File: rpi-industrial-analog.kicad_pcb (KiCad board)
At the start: 2 copper layers, 88.4 x 50 mm, 74 parts, among them J101 CONN_01X04, J102 CONN_01X08, U101 MCP3424, U102 ICL7660S,A, U103 AD8220, U104 AD8220, U105 AD8220, U106 AD8220

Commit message: added 3d file for phoenix connector
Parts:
- J102: footprint 3ML_Footprint_Library:1935226 -> 1935226
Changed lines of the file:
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@@
   )
   (setup
-    (last_trace_width 0.1524)
+    (last_trace_width 0.254)
     (user_trace_width 0.254)
     (user_trace_width 2.032)
@@
     (add_net "Net-(R106-Pad1)")
   )
+  (module 1935226 (layer F.Cu)
+    (at 188.341 115.758 90)
+    (fp_text reference J102 (at -5.588 -5.08 90) (layer F.SilkS)
+      (effects (font (size 1 1) (thickness 0.15)))
+    )
+    (fp_text value CONN_01X08 (at 12.7 6.096 90) (layer F.Fab) hide
+      (effects (font (size 1 1) (thickness 0.15)))
+    )
+    (fp_line (start 12.7 -4.064) (end 32.512 -4.064) (layer F.SilkS) (width 0.15))
+    (fp_line (start 12.7 4.064) (end 32.512 4.064) (layer F.SilkS) (width 0.15))
+    (fp_arc (start 12.7 4.064) (end 10.16 4.064) (angle 180) (layer F.SilkS) (width 0.15))
+    (fp_line (start -5.08 -4.064) (end 10.16 -4.064) (layer F.SilkS) (width 0.15))
+    (fp_line (start 12.7 4.064) (end -5.08 4.064) (layer F.SilkS) (width 0.15))
+    (fp_line (start 32.512 -4.064) (end 32.512 4.064) (layer F.SilkS) (width 0.15))
+    (fp_line (start 10.16 -4.064) (end 12.7 -4.064) (layer F.SilkS) (width 0.15))
+    (fp_line (start -7.62 4.064) (end -5.08 4.064) (layer F.SilkS) (width 0.15))
+    (fp_line (start -7.62 -4.064) (end -7.62 4.064) (layer F.SilkS) (width 0.15))
+    (fp_line (start -5.08 -4.064) (end -7.62 -4.064) (layer F.SilkS) (width 0.15))
+    (pad 8 thru_hole circle (at 30 0 90) (size 2 2) (drill 1.3) (layers *.Cu *.Mask)
+      (net 13 /AIN4-))
+    (pad 7 thru_hole circle (at 25 0 90) (size 2 2) (drill 1.3) (layers *.Cu *.Mask)
+      (net 17 /AIN4+))
+    (pad 6 thru_hole circle (at 20 0 90) (size 2 2) (drill 1.3) (layers *.Cu *.Mask)
+      (net 11 /AIN3-))
+    (pad 5 thru_hole circle (at 15 0 90) (size 2 2) (drill 1.3) (layers *.Cu *.Mask F.Paste)
+      (net 16 /AIN3+))
+    (pad 2 thru_hole circle (at 0 0 90) (size 2 2) (drill 1.3) (layers *.Cu *.Mask)
+      (net 7 /AIN1-))
+    (pad 1 thru_hole circle (at -5 0 90) (size 2 2) (drill 1.3) (layers *.Cu *.Mask)
+      (net 14 /AIN1+))
+    (pad 3 thru_hole circle (at 5 0 90) (size 2 2) (drill 1.3) (layers *.Cu *.Mask)
+      (net 15 /AIN2+))
+    (pad 4 thru_hole circle (at 10 0 90) (size 2 2) (drill 1.3) (layers *.Cu *.Mask)
+      (net 9 /AIN2-))
+    (model "${KIPRJMOD}/Hardware Libraries/3D/1935226.wrl"
+      (at (xyz -0.2 -1.74 -1.52))
+      (scale (xyz 0.39 0.39 0.39))
+      (rotate (xyz 90 180 90))
+    )
+  )
   (module Capacitors_SMD:C_0805 (layer F.Cu)
     (at 135.89 102.87)
@@
       (net 14 /AIN1+))
   )
-  (module 3ML_Footprint_Library:1935226 (layer F.Cu)
-    (at 188.341 115.758 90)
-    (fp_text reference J102 (at -8.956 -0.381 180) (layer F.SilkS)
-      (effects (font (size 1 1) (thickness 0.15)))
-    )
-    (fp_text value CONN_01X08 (at 12.7 6.096 90) (layer F.Fab) hide
-      (effects (font (size 1 1) (thickness 0.15)))
-    )
-    (fp_line (start 12.7 -4.064) (end 32.512 -4.064) (layer F.SilkS) (width 0.15))
-    (fp_line (start 12.7 4.064) (end 32.512 4.064) (layer F.SilkS) (width 0.15))
-    (fp_arc (start 12.7 4.064) (end 10.16 4.064) (angle 180) (layer F.SilkS) (width 0.15))
-    (fp_line (start -5.08 -4.064) (end 10.16 -4.064) (layer F.SilkS) (width 0.15))
-    (fp_line (start 12.7 4.064) (end -5.08 4.064) (layer F.SilkS) (width 0.15))
-    (fp_line (start 32.512 -4.064) (end 32.512 4.064) (layer F.SilkS) (width 0.15))
-    (fp_line (start 10.16 -4.064) (end 12.7 -4.064) (layer F.SilkS) (width 0.15))
-    (fp_line (start -7.62 4.064) (end -5.08 4.064) (layer F.SilkS) (width 0.15))
-    (fp_line (start -7.62 -4.064) (end -7.62 4.064) (layer F.SilkS) (width 0.15))
-    (fp_line (start -5.08 -4.064) (end -7.62 -4.064) (layer F.SilkS) (width 0.15))
-    (pad 8 thru_hole circle (at 30 0 90) (size 2 2) (drill 1.3) (layers *.Cu *.Mask)
-      (net 13 /AIN4-))
-    (pad 7 thru_hole circle (at 25 0 90) (size 2 2) (drill 1.3) (layers *.Cu *.Mask)
-      (net 17 /AIN4+))
-    (pad 6 thru_hole circle (at 20 0 90) (size 2 2) (drill 1.3) (layers *.Cu *.Mask)
-      (net 11 /AIN3-))
-    (pad 5 thru_hole circle (at 15 0 90) (size 2 2) (drill 1.3) (layers *.Cu *.Mask F.Paste)
-      (net 16 /AIN3+))
-    (pad 2 thru_hole circle (at 0 0 90) (size 2 2) (drill 1.3) (layers *.Cu *.Mask)
-      (net 7 /AIN1-))
-    (pad 1 thru_hole circle (at -5 0 90) (size 2 2) (drill 1.3) (layers *.Cu *.Mask)
-      (net 14 /AIN1+))
-    (pad 3 thru_hole circle (at 5 0 90) (size 2 2) (drill 1.3) (layers *.Cu *.Mask)
-      (net 15 /AIN2+))
-    (pad 4 thru_hole circle (at 10 0 90) (size 2 2) (drill 1.3) (layers *.Cu *.Mask)
-      (net 9 /AIN2-))
-  )
   (module 3ML_Footprint_Library:3ML_LOGO (layer F.Cu)
     (at 109.728 88.392)
@@
   (segment (start 181.229 108.061) (end 185.644 108.061) (width 0.254) (layer F.Cu) (net 15) (status 10))
   (segment (start 185.644 108.061) (end 188.341 110.758) (width 0.254) (layer F.Cu) (net 15) (status 20))
+  (segment (start 183.332 100.758) (end 188.341 100.758) (width 0.254) (layer F.Cu) (net 16))
   (segment (start 168.021 96.713) (end 164.206 96.713) (width 0.254) (layer F.Cu) (net 16) (status 30))
   (segment (start 164.206 96.713) (end 163.891 97.028) (width 0.254) (layer F.Cu) (net 16) (status 30))
@@
   (segment (start 178.451 98.028) (end 177.038 99.441) (width 0.254) (layer F.Cu) (net 16))
   (segment (start 177.038 99.441) (end 177.038 100.584) (width 0.254) (layer F.Cu) (net 16) (status 20))
-  (segment (start 188.341 100.758) (end 183.332 100.758) (width 0.254) (layer F.Cu) (net 16) (status 10))
   (segment (start 183.332 100.758) (end 181.356 98.782) (width 0.254) (layer F.Cu) (net 16))
   (segment (start 181.356 98.782) (end 181.356 98.028) (width 0.254) (layer F.Cu) (net 16) (status 20))

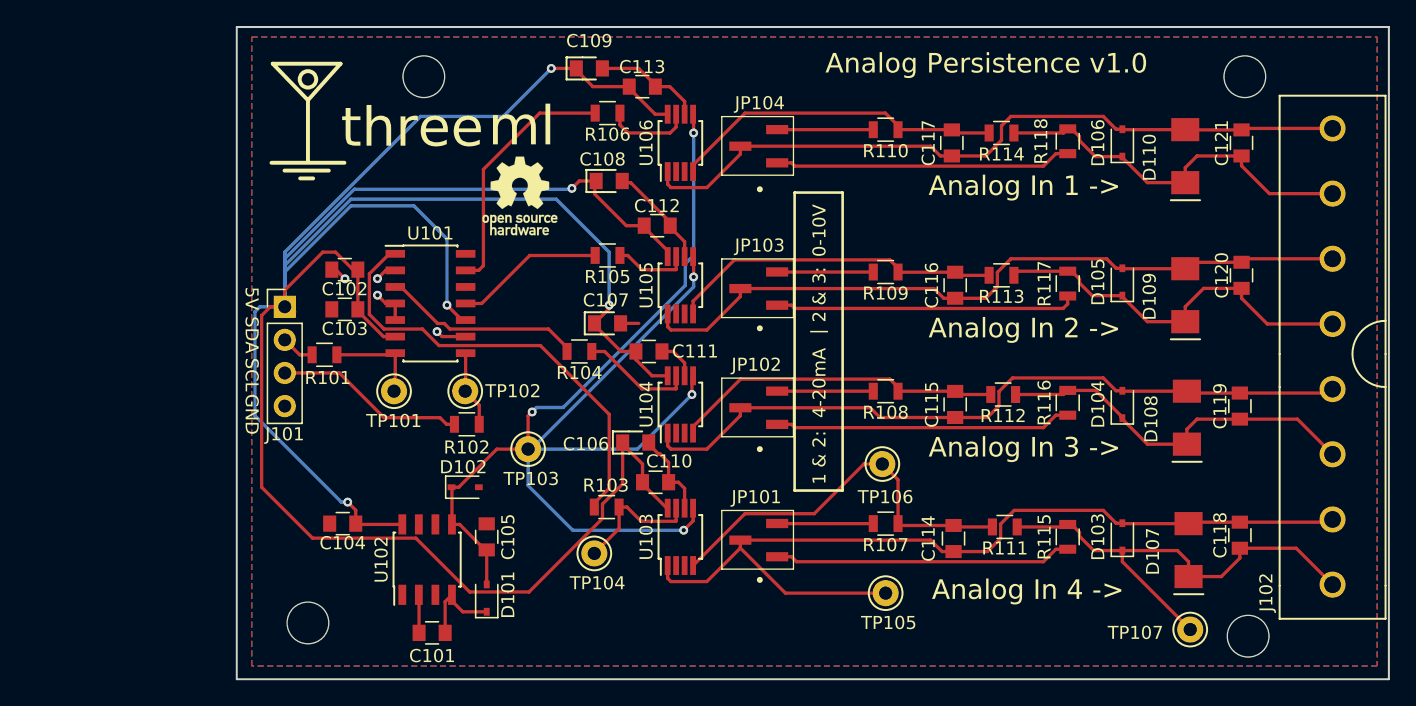
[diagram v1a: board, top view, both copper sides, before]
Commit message: revised board for production and added 1M caps so that this thing works
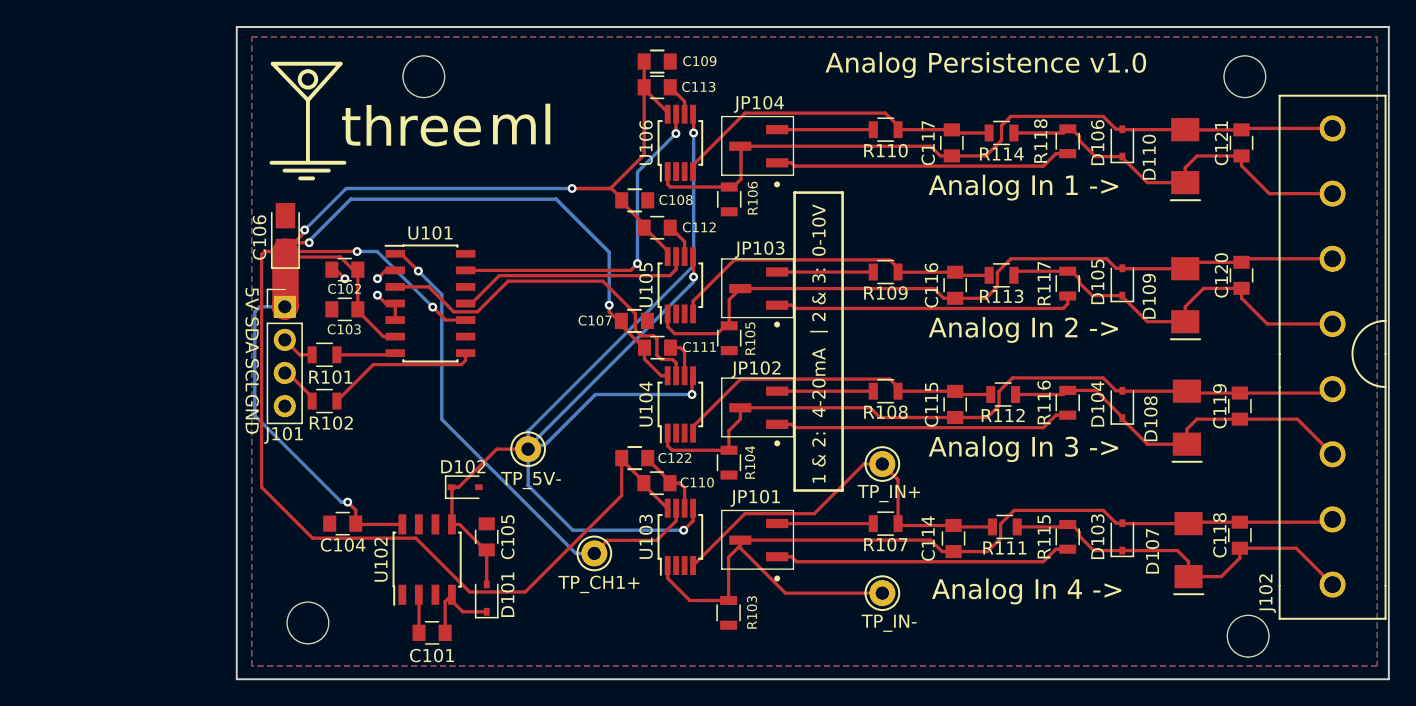
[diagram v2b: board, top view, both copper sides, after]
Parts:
- removed ACC102: ACC_?, Symbols:OSHW-Logo_5.7x6mm_SilkScreen
- removed TP101: TEST SDA, 3ML_Footprint_Library:Keystone_5000_Test_Point_Mini
- removed TP102: TEST SDL, 3ML_Footprint_Library:Keystone_5000_Test_Point_Mini
- removed TP107: TEST IN+ DIODES, 3ML_Footprint_Library:Keystone_5000_Test_Point_Mini
- added C122: 10uF, Capacitors_SMD:C_0805, F.Cu at (134.8, 111.0)
- C106: footprint 3ML_Footprint_Library:C_0805_POL -> Capacitors_Tantalum_SMD:CP_Tantalum_Case-A_EIA-3216-18_Reflow
- C107, C108, C109: footprint 3ML_Footprint_Library:C_0805_POL -> Capacitors_SMD:C_0805
- J102: footprint 1935226 -> 3ML_Footprint_Library:1935226
- R103, R104, R105, R106: value 10K -> 1M
- moved C106 31.3 mm to (108.0, 93.8), turned to 90 degrees
- moved R104 14.3 mm to (142.0, 111.4), turned to 270 degrees
- moved R103 12.4 mm to (142.0, 122.9), turned to 270 degrees
- moved R106 11.4 mm to (142.1, 91.2), turned to 270 degrees
- moved R105 11.3 mm to (142.1, 101.8), turned to 270 degrees
- moved R102 11.1 mm to (111.0, 106.7)
- moved C109 5.23 mm to (136.5, 80.6)
- moved C108 2.46 mm to (134.8, 91.3)
- moved C107 2.07 mm to (134.8, 100.5)
- moved C113 1.14 mm to (136.5, 82.6)
- moved C111 0.72 mm to (136.6, 102.6)
- moved TP_IN- 0.25 mm to (153.8, 121.4)
- moved C112 0.16 mm to (136.5, 93.4)
- moved C110 0.12 mm to (136.5, 113.0)
- renumbered TP103 to TP_5V-, TP104 to TP_CH1+, TP106 to TP_IN+, TP105 to TP_IN-
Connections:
- R103 pad 1: Net-(R103-Pad1) -> /AIN1-
- R103 pad 2: /CH1+ -> GND
- R104 pad 1: Net-(R104-Pad1) -> /AIN2-
- R104 pad 2: /CH2+ -> GND
- R105 pad 1: Net-(R105-Pad1) -> /AIN3-
- R105 pad 2: /CH3+ -> GND
- R106 pad 1: Net-(R106-Pad1) -> /AIN4-
- R106 pad 2: /CH4+ -> GND
- TP_CH1+ pad 1: Net-(R103-Pad1) -> /CH1+
- U103 pad 7: Net-(R103-Pad1) -> /CH1+
- U104 pad 7: Net-(R104-Pad1) -> /CH2+
- U105 pad 7: Net-(R105-Pad1) -> /CH3+
- U106 pad 7: Net-(R106-Pad1) -> /CH4+
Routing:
- net +5V: track 251.1 -> 213.3 mm, vias 5 -> 7
- net GND: track 36.3 -> 21.3 mm, vias 4 -> 3
- net /CH2+: track 15.9 -> 28.9 mm
- net /SCL: track 15.2 -> 3.71 mm
- net Net-(R103-Pad1): track 10.2 -> 0.00 mm
- net Net-(R104-Pad1): track 8.65 -> 0.00 mm
- net /AIN1+: track 37.5 -> 29.3 mm
- net Net-(R106-Pad1): track 6.94 -> 0.00 mm
- net /CH4+: track 19.3 -> 26.1 mm, vias 0 -> 2
- net /CH3+: track 11.5 -> 18.2 mm
- net Net-(R105-Pad1): track 5.75 -> 0.00 mm
- net Net-(R102-Pad2): track 6.78 -> 12.2 mm
- net /CH1+: track 34.9 -> 39.1 mm, vias 0 -> 1
- net Net-(R101-Pad1): track 7.94 -> 4.76 mm
- net /AIN1-: track 69.1 -> 72.0 mm
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
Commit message: adding gerbers, fixing DRC, adding overvoltage diodes to MCP inputs
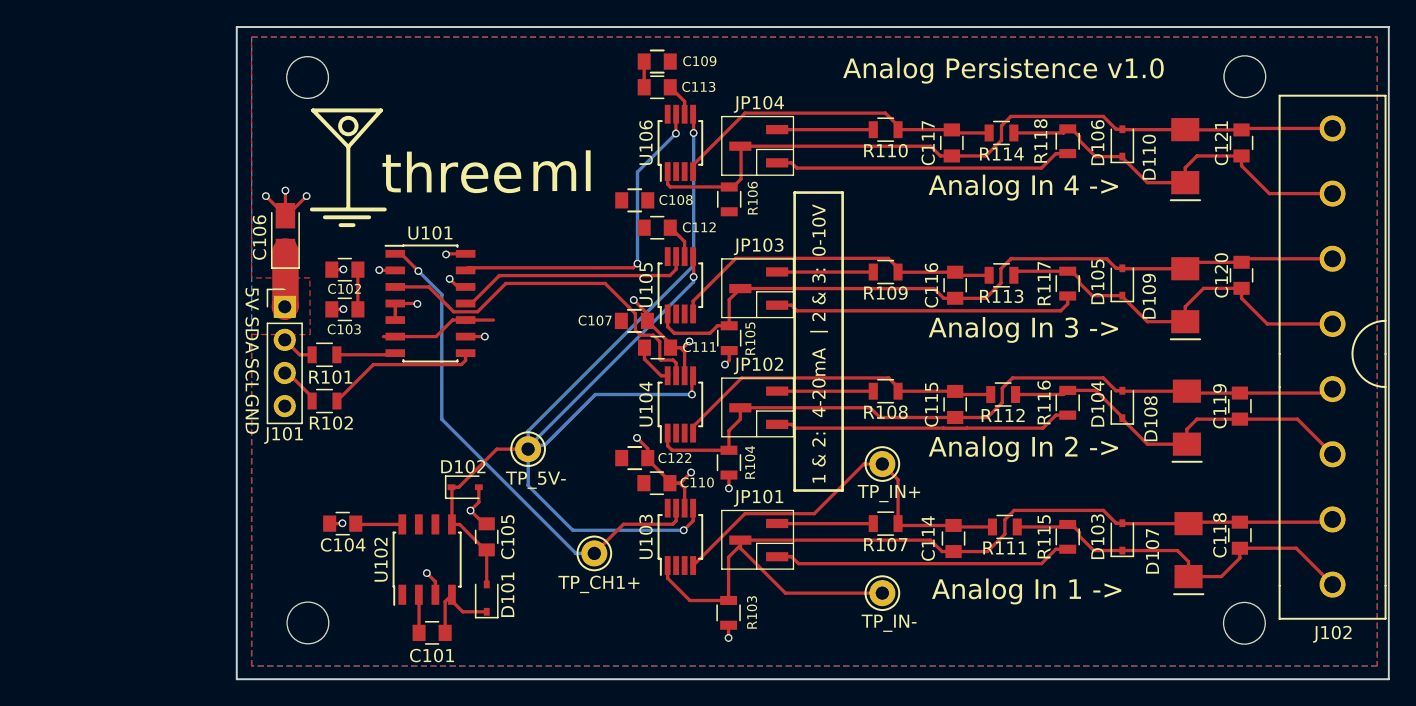
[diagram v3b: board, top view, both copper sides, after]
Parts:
- JP104: footprint 3ML_Footprint_Library:GRPB031VWTC-RC_3pos_Header -> GRPB031VWTC-RC_3pos_Header
- moved ACC105 8.92 mm to (109.7, 81.8)
- moved LG101 4.74 mm to (112.8, 92.0)
- moved ACC104 1.03 mm to (181.6, 123.7)
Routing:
- net +5V: track 213.3 -> 30.4 mm, vias 7 -> 0
- net GND: track 21.3 -> 52.7 mm, vias 3 -> 20
- added copper zone on F.Cu, net +5V
- removed copper zone on F.Cu, net GND
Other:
- net class Default: clearance 0.1524 -> 0.2; trace_width 0.1524 -> 0.25; via_dia 0.6858 -> 0.6; via_drill 0.3302 -> 0.4
- rule trace_clearance: 0.1524 -> 0.2
- rule trace_min: 0.1524 -> 0.25
- rule via_min_drill: 0.3302 -> 0.305
- rule via_min_size: 0.6858 -> 0.6

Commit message: cleaning-up Gerbers and step 1 of migrating footprints to master 3ML library
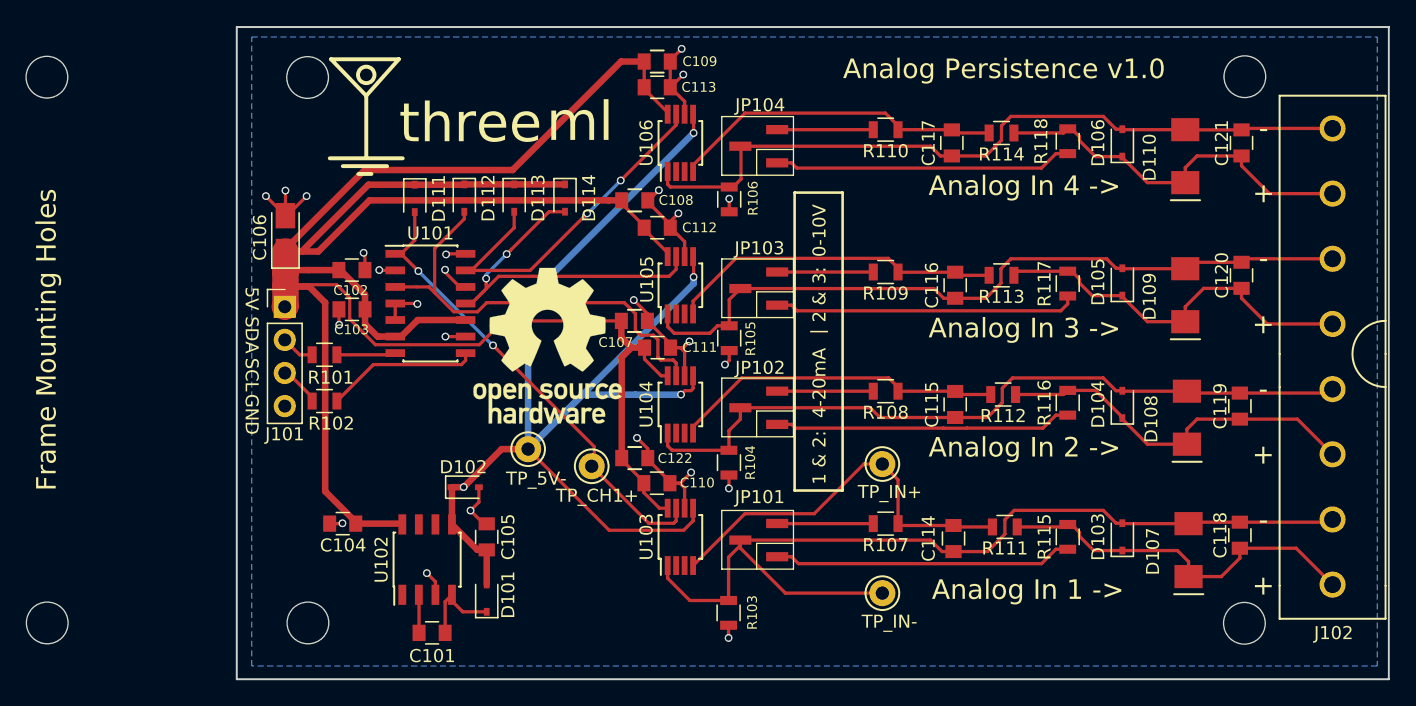
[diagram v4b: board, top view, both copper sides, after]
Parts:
- added ACC101: ACC_?, Mounting_Holes:MountingHole_3.2mm_M3_DIN965, F.Cu at (89.7, 123.7)
- added ACC105: ACC_?, Mounting_Holes:MountingHole_3.2mm_M3_DIN965, F.Cu at (89.7, 81.8)
- added ACC109: ACC_?, Symbols:OSHW-Logo_11.4x12mm_SilkScreen, F.Cu at (128.1, 102.4)
- added D111: D_Schottky_Small_ALT, Diodes_SMD:D_SOD-323, F.Cu at (117.9, 91.1)
- added D112: D_Schottky_Small_ALT, Diodes_SMD:D_SOD-323, F.Cu at (121.7, 91.1)
- added D113: D_Schottky_Small_ALT, Diodes_SMD:D_SOD-323, F.Cu at (125.5, 91.1)
- added D114: D_Schottky_Small_ALT, Diodes_SMD:D_SOD-323, F.Cu at (129.4, 91.1)
- moved TP_CH1+ 6.69 mm to (131.5, 111.7)
- moved LG101 4.16 mm to (114.2, 88.0)
- moved C103 0.55 mm to (113.1, 99.6)
- moved C102 0.54 mm to (113.1, 96.6), turned to 0 degrees
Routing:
- net +5V: track 30.4 -> 199.3 mm
- net GND: track 52.7 -> 65.5 mm, vias 20 -> 25
- net /CH3+: track 18.2 -> 28.9 mm, vias 0 -> 2
- net /CH2+: track 28.8 -> 34.7 mm
- net /CH1+: track 39.1 -> 36.3 mm, vias 1 -> 2
- net /CH4+: track 26.1 -> 28.5 mm
- removed copper zone on F.Cu, net +5V
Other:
- board text added: "+"
- board text added: "-"
- board text added: "Frame Mounting Holes"

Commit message: updating footprints to use master library
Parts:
- U102: value ICL7660S,A -> ICL7660S A
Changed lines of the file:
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@@
 (kicad_pcb (version 4) (host pcbnew 4.0.6)
   (general
-    (links 146)
-    (no_connects 0)
-    (area 86.424999 77.013 195.512 134.425)
+    (links 150)
+    (no_connects 4)
+    (area 104.191999 77.902999 192.734001 128.091001)
     (thickness 1.6)
     (drawings 35)
@@
       (effects (font (size 1 1) (thickness 0.15)))
     )
-    (fp_text value ICL7660S,A (at 0 3.5 90) (layer F.Fab)
-      (effects (font (size 1 1) (thickness 0.15)))
-    )
+    (fp_text value "ICL7660S A" (at 0 3.5 90) (layer F.Fab)
+      (effects (font (size 1 1) (thickness 0.15)))
+    )
